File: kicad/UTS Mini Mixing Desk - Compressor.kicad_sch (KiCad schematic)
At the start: 0 parts

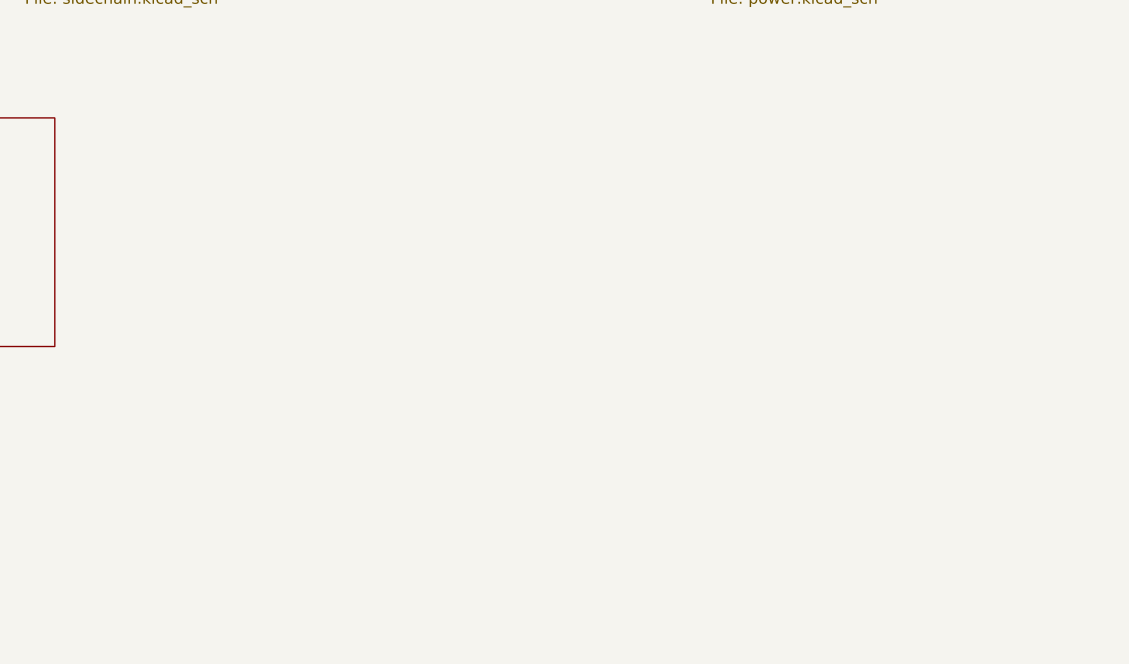
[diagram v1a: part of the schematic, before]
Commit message: Make the schematic simulate in KiCad, and add the simulation results
Every part on the kicad/ sheets now has a SPICE model (Sim.* fields, models in
kicad/sim/compressor_models.lib), the connectors are excluded from simulation, and the
root sheet carries a test bench: the rack's supplies, a balanced source, a load and the
knob settings as .param lines. The netlist is unchanged.

tools/add_sim_models.py writes the fields. tools/sim/run_all.py exports the netlist with
kicad-cli and runs the characterisation in ngspice; kicad/sim/README.md has how to run
it in KiCad and what it found.
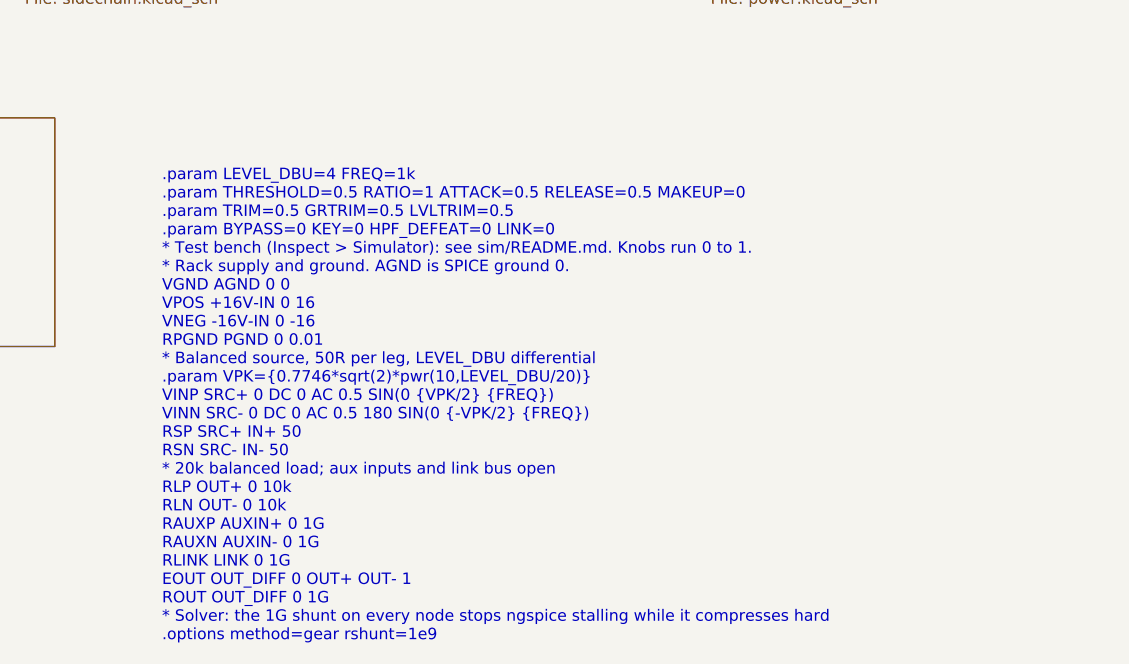
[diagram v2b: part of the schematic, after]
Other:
- note added: ".param LEVEL_DBU=4 FREQ=1k .param THRESHOLD=0.5 RATIO=1 ATTACK=0.5 RELEASE=0.5 MAKEUP=0 .param TRIM=0.5 GRTRIM=0.5 LVLTRIM=0.5 .param BYPASS=0 KEY=0 HPF_DEFEAT=0 LINK=0 * Test bench (Inspect > Simulator): see sim/README.md. Knobs run 0 to 1. * Rack supply and ground. AGND is SPICE ground 0. VGND AGND 0 0 VPOS +16V-IN 0 16 VNEG -16V-IN 0 -16 RPGND PGND 0 0.01 * Balanced source, 50R per leg, LEVEL_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"
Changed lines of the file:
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@@
 		(company "UTS Mini Mixing Desk")
+	)
+	(text ".param LEVEL_DBU=4 FREQ=1k\n.param THRESHOLD=0.5 RATIO=1 ATTACK=0.5 RELEASE=0.5 MAKEUP=0\n.param TRIM=0.5 GRTRIM=0.5 LVLTRIM=0.5\n.param BYPASS=0 KEY=0 HPF_DEFEAT=0 LINK=0\n* Test bench (Inspect > Simulator): see sim/README.md. Knobs run 0 to 1.\n* Rack supply and ground. AGND is SPICE ground 0.\nVGND AGND 0 0\nVPOS +16V-IN 0 16\nVNEG -16V-IN 0 -16\nRPGND PGND 0 0.01\n* Balanced source, 50R per leg, LEVEL_DBU differential\n.param VPK={0.7746*sqrt(2)*pwr(10,LEVEL_DBU/20)}\nVINP SRC+ 0 DC 0 AC 0.5 SIN(0 {VPK/2} {FREQ})\nVINN SRC- 0 DC 0 AC 0.5 180 SIN(0 {-VPK/2} {FREQ})\nRSP SRC+ IN+ 50\nRSN SRC- IN- 50\n* 20k balanced load; aux inputs and link bus open\nRLP OUT+ 0 10k\nRLN OUT- 0 10k\nRAUXP AUXIN+ 0 1G\nRAUXN AUXIN- 0 1G\nRLINK LINK 0 1G\nEOUT OUT_DIFF 0 OUT+ OUT- 1\nROUT OUT_DIFF 0 1G\n* Solver: the 1G shunt on every node stops ngspice stalling while it compresses hard\n.options method=gear rshunt=1e9"
+		(exclude_from_sim no)
+		(at 140.97 142.24 0)
+		(effects
+			(font
+				(size 1.27 1.27)
+			)
+			(justify left top)
+		)
 	)
 	(text "UTS Mini Mixing Desk - Compressor - one sheet per section"
